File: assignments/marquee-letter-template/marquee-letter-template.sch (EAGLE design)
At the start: 2 parts

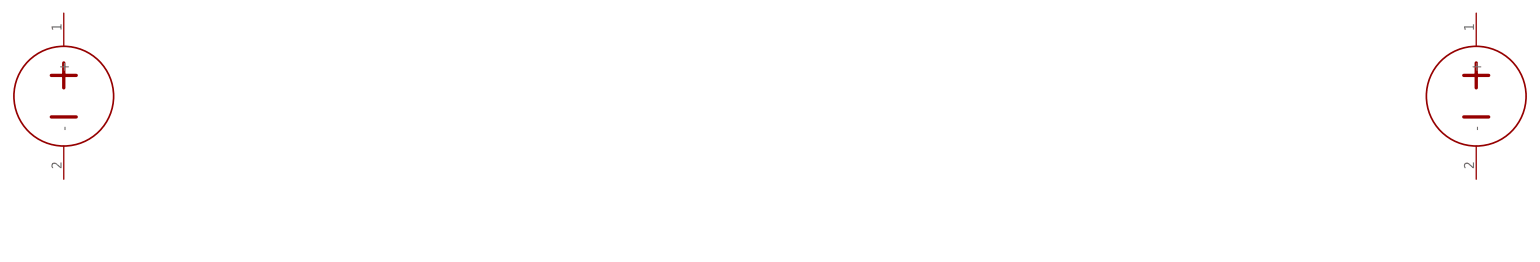
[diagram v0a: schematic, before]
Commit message: marquee template; schematic images
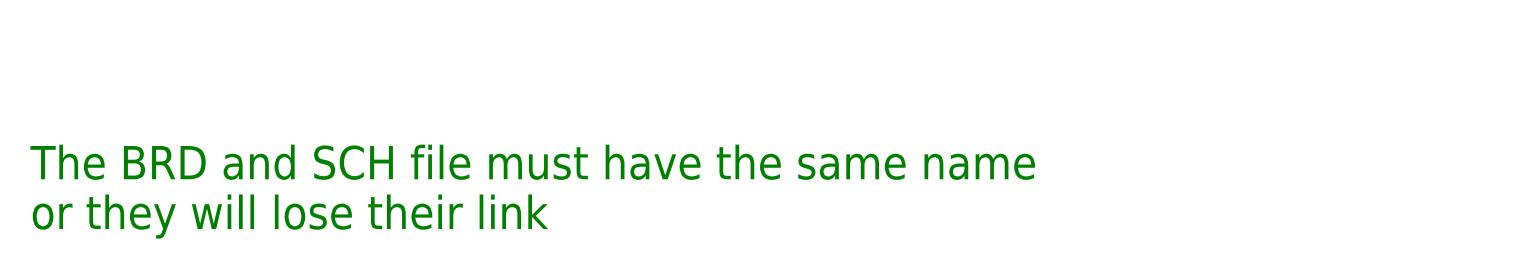
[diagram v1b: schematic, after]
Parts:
- removed U$1, U$2: CONN_BATTERY-LIPO-HORIZ, homemade-hardware:CONN_BATTERY-LIPO-HORIZ
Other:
- note added: "The BRD and SCH file must have the same name or they will lose their link"
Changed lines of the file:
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@@
 </classes>
 <parts>
-<part name="U$1" library="homemade-hardware" deviceset="CONN_BATTERY" device="-LIPO-HORIZ"/>
-<part name="U$2" library="homemade-hardware" deviceset="CONN_BATTERY" device="-LIPO-HORIZ"/>
 </parts>
 <sheets>
 <sheet>
 <plain>
+<text x="5.08" y="7.62" size="5.08" layer="91">The BRD and SCH file must have the same name
+or they will lose their link</text>
 </plain>
 <instances>
-<instance part="U$1" gate="G$1" x="10.16" y="27.94" smashed="yes"/>
-<instance part="U$2" gate="G$1" x="226.06" y="27.94" smashed="yes"/>
 </instances>
 <busses>
@@
 </schematic>
 </drawing>
+<compatibility>
+<note version="6.3" minversion="6.2.2" severity="warning">
+Since Version 6.2.2 text objects can contain more than one line,
+which will not be processed correctly with this version.
+</note>
+</compatibility>
 </eagle>
